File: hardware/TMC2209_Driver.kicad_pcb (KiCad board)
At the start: 2 copper layers, 36.7 x 39.4 mm, 29 parts, among them J1 PCIe_Stepper, J2 Conn_01x04_Male, U1 TMC2209-LA, U2 74LVC1G06, U3 24LC02

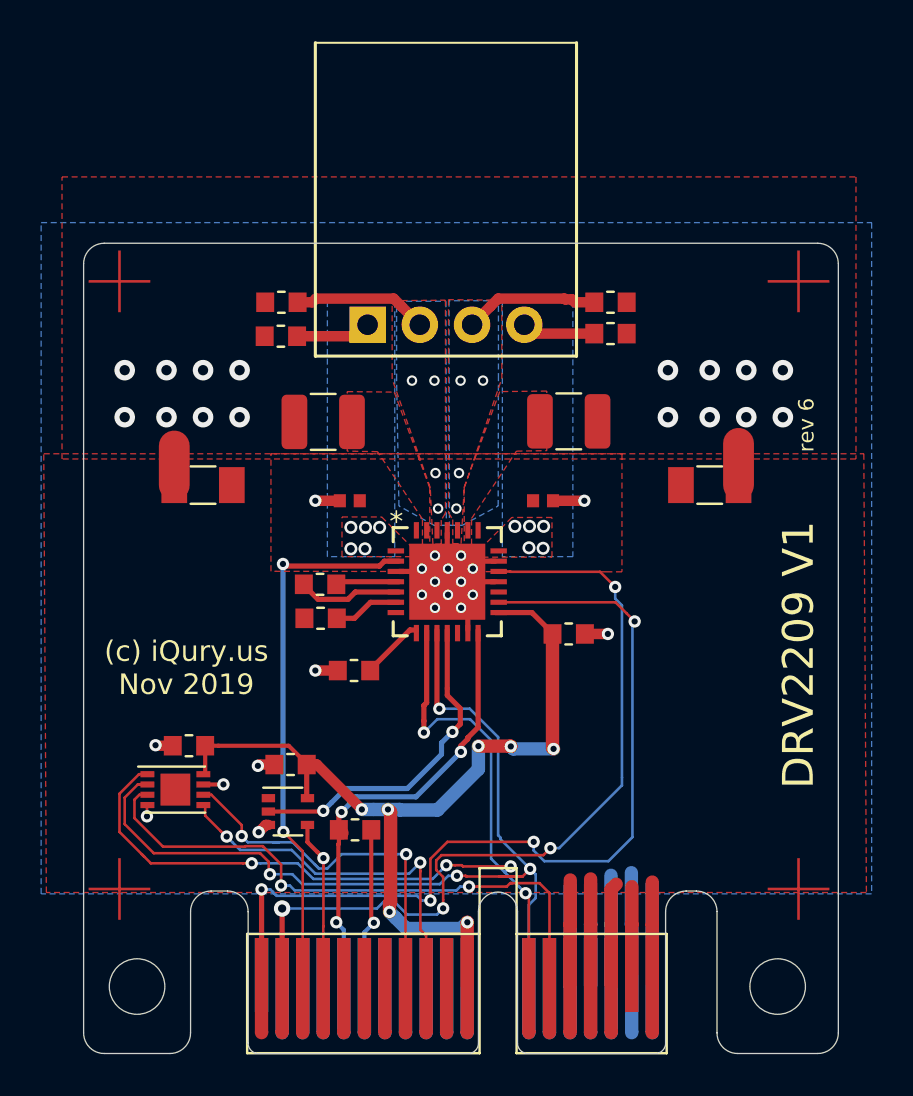
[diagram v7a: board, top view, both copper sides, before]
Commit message: Update TMC2209 DRC to 6mil spec.
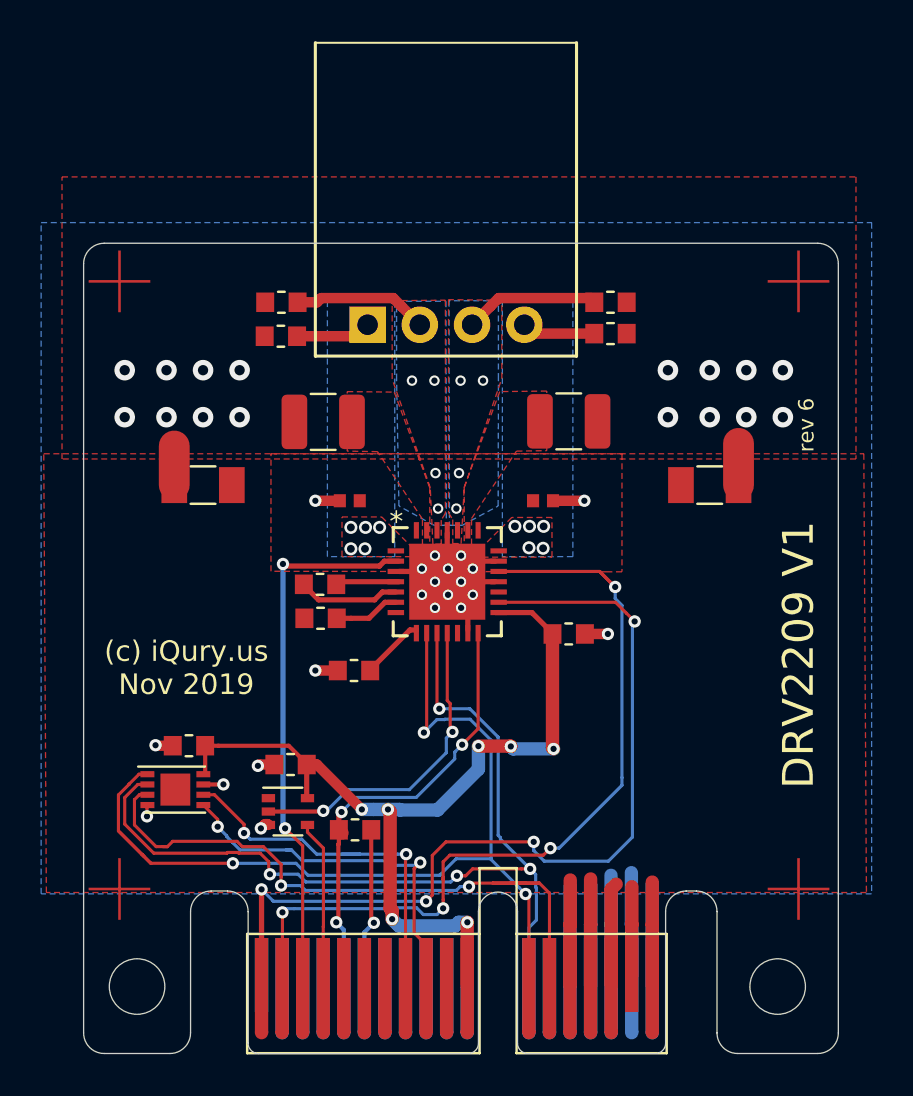
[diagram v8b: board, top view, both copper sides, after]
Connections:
- J1 pad : /~ENABLE -> (no net)
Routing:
- net /ID_2: track 28.7 -> 32.4 mm
- net /ID_1: track 45.9 -> 44.6 mm
- net /ID_0: track 46.4 -> 46.9 mm, vias 5 -> 3
- net /ALARM1: track 8.32 -> 8.12 mm, vias 1 -> 0
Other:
- net class Default: clearance 0.127 -> 0.1524
- rule trace_clearance: 0.127 -> 0.1524
- rule trace_min: 0.127 -> 0.1524
- rule via_min_drill: 0.2 -> 0.254
- rule via_min_size: 0.45 -> 0.508
